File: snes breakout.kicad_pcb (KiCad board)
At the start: 2 copper layers, 100 x 44 mm, 13 parts, among them J1 Conn_01x12_Male, J2 Mini-DIN-4, J3 Conn_01x09_Female, J4 DB15_Female_HighDensity_Mount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, J5 AudioJack3

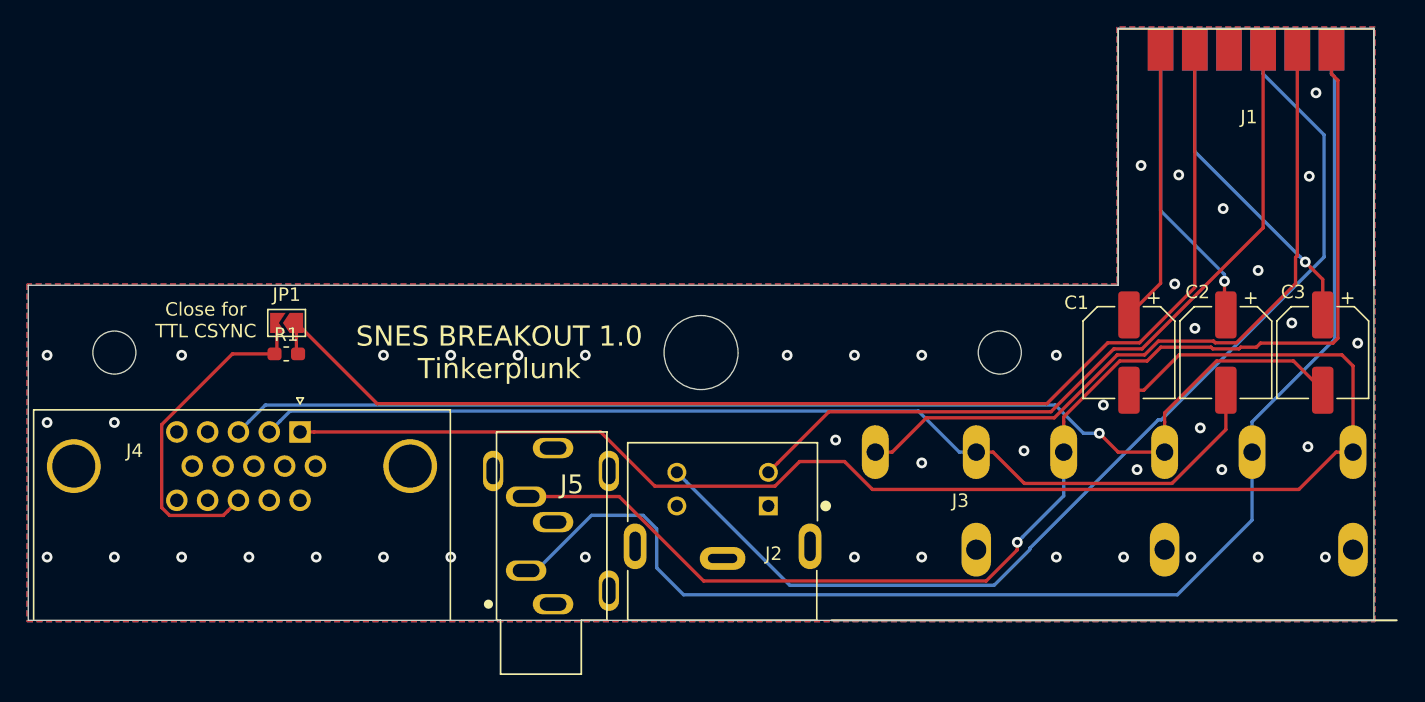
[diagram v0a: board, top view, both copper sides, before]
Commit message: Fixes
Fixed routing, removed some mask on the bottom to solder the spring on. Ready for action.
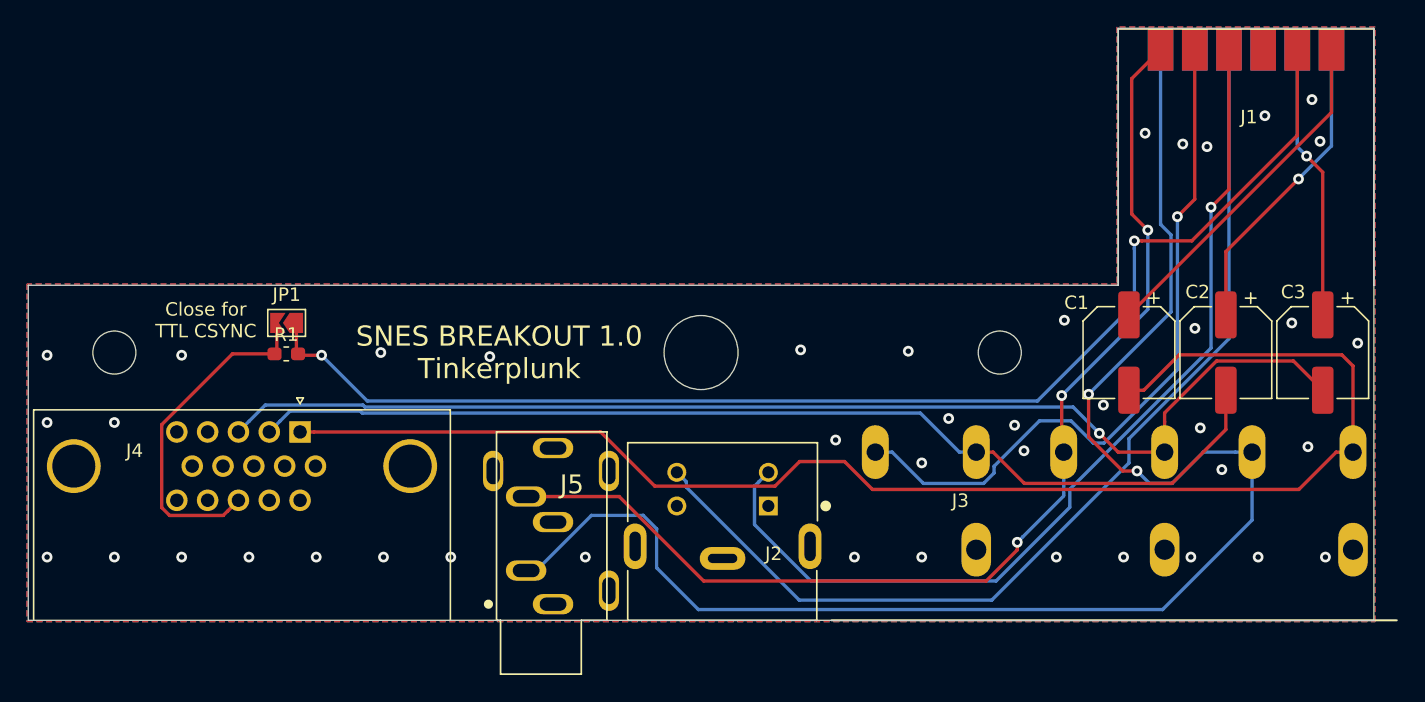
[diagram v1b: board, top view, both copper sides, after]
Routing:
- net RIGHT: track 99.7 -> 114.8 mm, vias 0 -> 2
- net LEFT: track 96.9 -> 83.8 mm, vias 1 -> 3
- net LUMA: track 57.5 -> 70.6 mm, vias 0 -> 1
- net RED: track 20.7 -> 25.9 mm
- net CHROMA: track 79.0 -> 75.8 mm
- net BLUE: track 23.6 -> 20.5 mm
- net CSYNC: track 93.0 -> 95.5 mm, vias 0 -> 2
- net GREEN: track 21.7 -> 23.0 mm
- net CVBS: track 54.0 -> 52.9 mm, vias 0 -> 1
- net GND: vias 44 -> 42
- net (no net): vias 1 -> 0
